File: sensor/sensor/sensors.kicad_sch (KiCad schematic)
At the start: 28 parts, among them IC1 VL53L4CDV0DH_1, J4 Conn_01x03_Socket, J5 Conn_01x03_Socket, J6 Conn_01x03_Socket, J7 Conn_01x03_Socket, U3 APDS-9960, U4 PCA9536DP, U6 ICM-20602

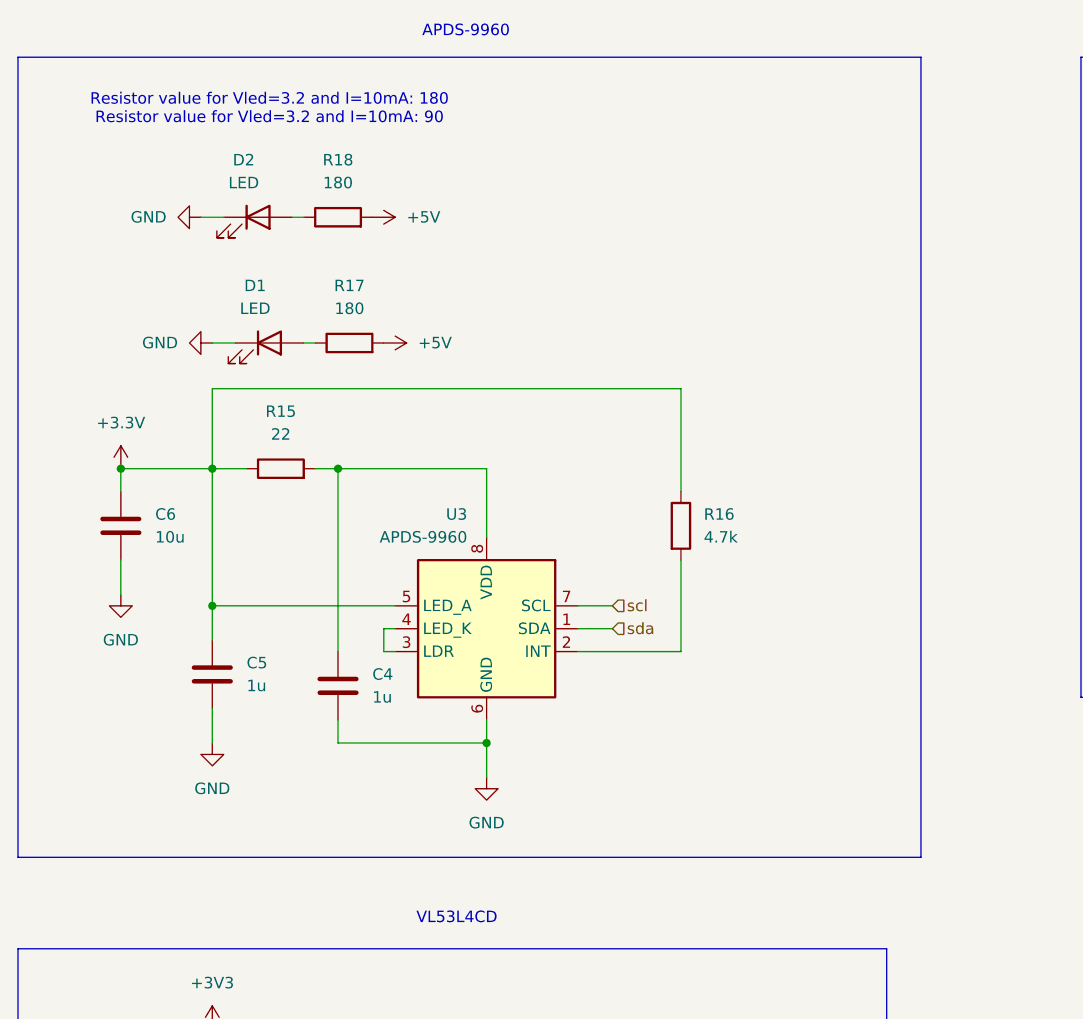
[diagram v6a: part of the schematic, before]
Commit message: update color sensor
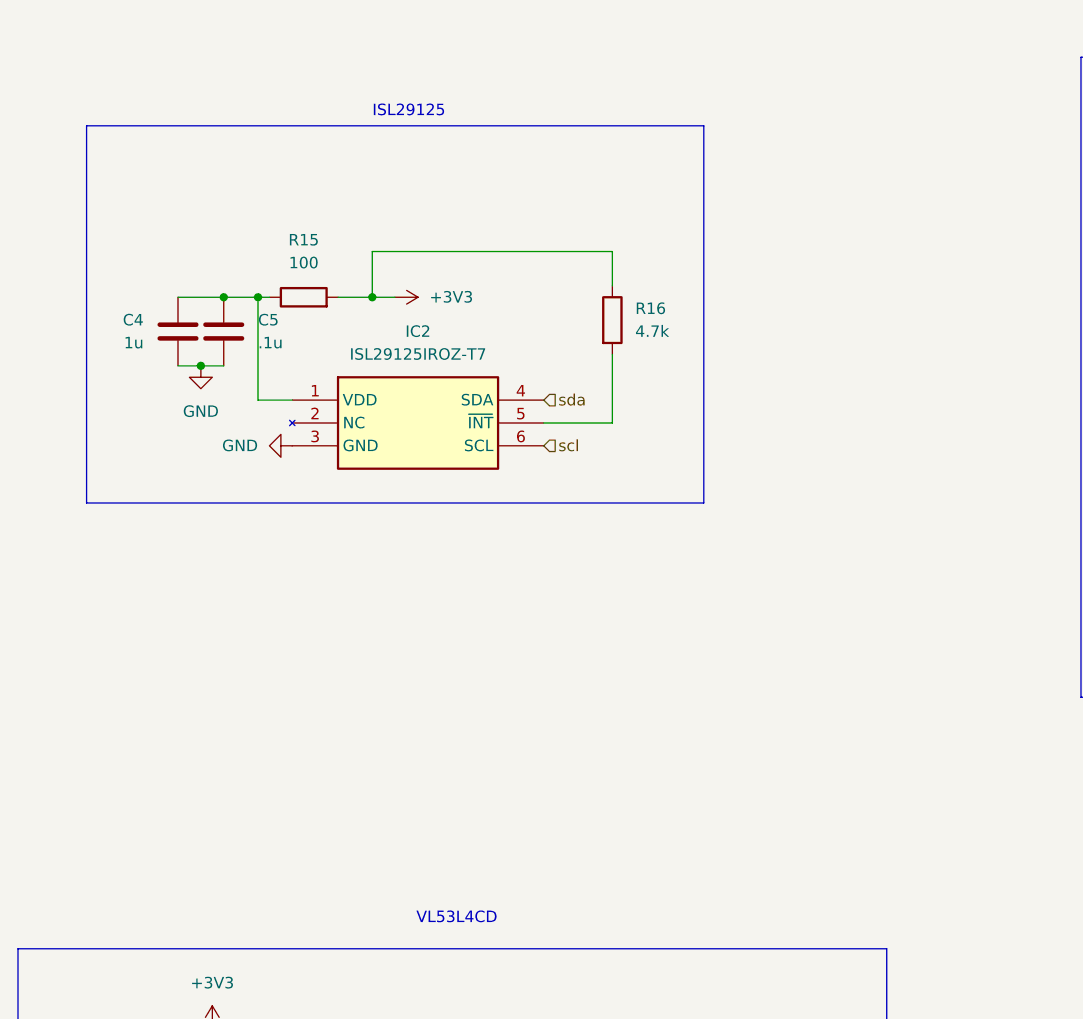
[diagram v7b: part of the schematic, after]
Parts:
- removed C6: 10u, Capacitor_SMD:C_0603_1608Metric_Pad1.08x0.95mm_HandSolder, symbol Device:C
- removed D1, D2: LED, LED_SMD:LED_0805_2012Metric_Pad1.15x1.40mm_HandSolder, symbol Device:LED
- removed R17, R18: 180, Resistor_SMD:R_0402_1005Metric_Pad0.72x0.64mm_HandSolder, symbol Device:R
- removed U3: APDS-9960, Sensor:Avago_APDS-9960, symbol Sensor:APDS-9960
- added IC2: ISL29125IROZ-T7, ISL29125IROZT7, symbol ISL29125:ISL29125IROZ-T7
- C4: footprint Capacitor_SMD:C_0603_1608Metric_Pad1.08x0.95mm_HandSolder -> (none)
- C5: value 1u -> .1u; footprint Capacitor_SMD:C_0603_1608Metric_Pad1.08x0.95mm_HandSolder -> (none)
- R15: value 22 -> 100; footprint Resistor_SMD:R_0402_1005Metric_Pad0.72x0.64mm_HandSolder -> (none)
- R16: footprint Resistor_SMD:R_0402_1005Metric_Pad0.72x0.64mm_HandSolder -> (none)
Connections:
- net +3.3V: no longer C5.1, R15.1, R16.1
- net +3V3: now also R15.2, R16.1
- net GND: now also IC2.3 (GND)
- net scl: now also IC2.6 (SCL)
- net sda: now also IC2.4 (SDA)
- net at R16.2: now also IC2.5 (~{INT})
- net at C4.1: now also C5.1, R15.1, IC2.1 (VDD); no longer R15.2
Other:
- note added: "ISL29125"
- note removed: "APDS-9960"
- note removed: "Resistor value for Vled=3.2 and I=10mA: 180 Resistor value for Vled=3.2 and I=10mA: 90"

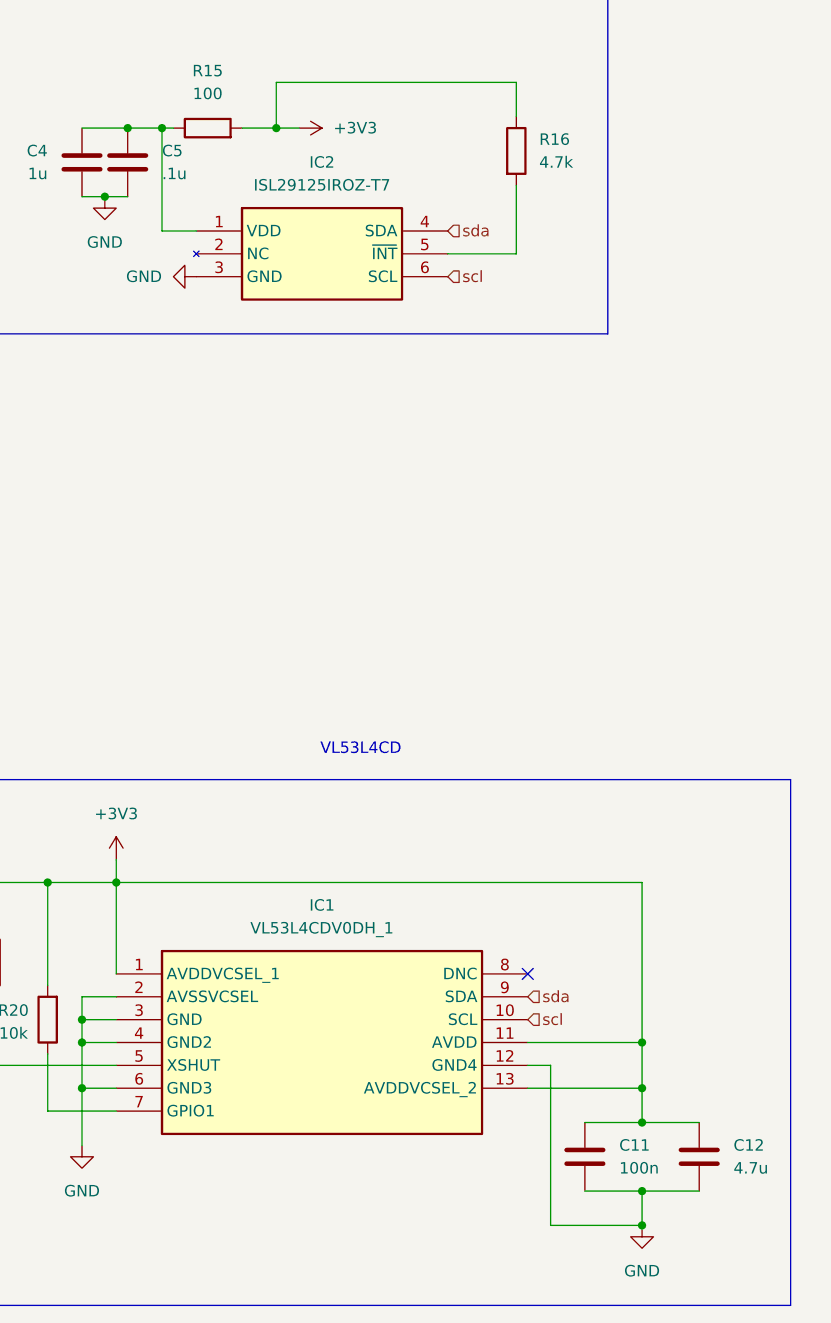
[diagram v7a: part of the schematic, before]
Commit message: added footprints of new sensors and JST/RJ12 connectors into PCB
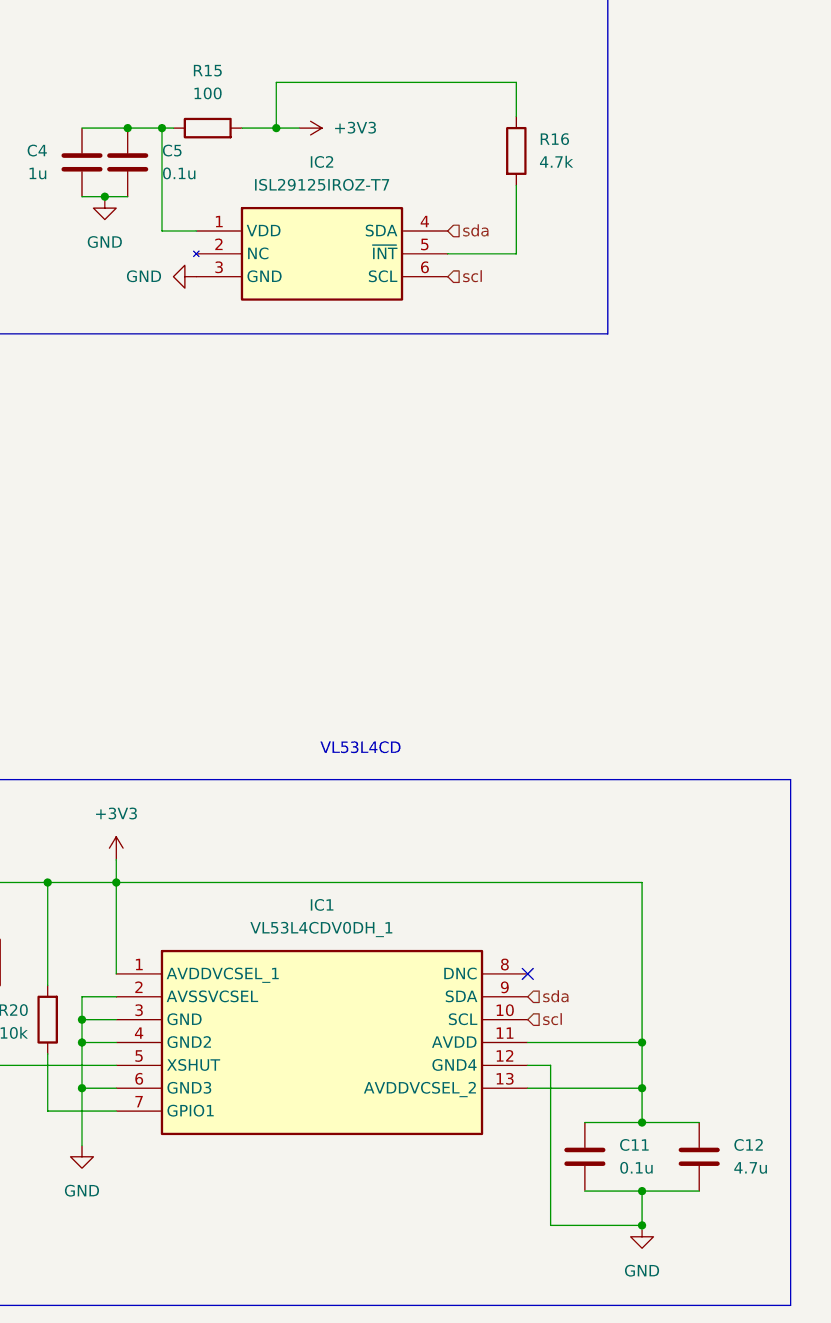
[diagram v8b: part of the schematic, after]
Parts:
- C11: value 100n -> 0.1u; footprint (none) -> Capacitor_SMD:C_0402_1005Metric_Pad0.74x0.62mm_HandSolder
- C12, C4: footprint (none) -> Capacitor_SMD:C_0603_1608Metric_Pad1.08x0.95mm_HandSolder
- C5: value .1u -> 0.1u; footprint (none) -> Capacitor_SMD:C_0402_1005Metric_Pad0.74x0.62mm_HandSolder
- IC1: footprint VL53L4CDV0DH1 -> VL53L4CD:VL53L4CDV0DH1
- IC2: footprint ISL29125IROZT7 -> ISL29125:ISL29125IROZT7
- R15, R16, R20, R21: footprint (none) -> Resistor_SMD:R_0402_1005Metric_Pad0.72x0.64mm_HandSolder
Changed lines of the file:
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@@
 			)
 		)
-		(property "Footprint" ""
+		(property "Footprint" "Capacitor_SMD:C_0603_1608Metric_Pad1.08x0.95mm_HandSolder"
 			(at 43.4848 63.5 0)
 			(effects
@@
 			)
 		)
-		(property "Footprint" ""
+		(property "Footprint" "Resistor_SMD:R_0402_1005Metric_Pad0.72x0.64mm_HandSolder"
 			(at 90.932 58.42 90)
 			(effects
@@
 			)
 		)
-		(property "Value" ".1u"
+		(property "Value" "0.1u"
 			(at 53.34 60.9599 0)
 			(effects
@@
 			)
 		)
-		(property "Footprint" ""
+		(property "Footprint" "Capacitor_SMD:C_0402_1005Metric_Pad0.74x0.62mm_HandSolder"
 			(at 50.4952 63.5 0)
 			(effects
@@
 			)
 		)
-		(property "Footprint" ""
+		(property "Footprint" "Resistor_SMD:R_0402_1005Metric_Pad0.72x0.64mm_HandSolder"
 			(at 42.418 154.94 90)
 			(effects
@@
 			)
 		)
-		(property "Footprint" "ISL29125IROZT7"
+		(property "Footprint" "ISL29125:ISL29125IROZT7"
 			(at 81.28 162.23 0)
 			(effects
@@
 			)
 		)
-		(property "Footprint" ""
+		(property "Footprint" "Capacitor_SMD:C_0603_1608Metric_Pad1.08x0.95mm_HandSolder"
 			(at 113.9952 173.99 0)
 			(effects
@@
 			)
 		)
-		(property "Footprint" ""
+		(property "Footprint" "Resistor_SMD:R_0402_1005Metric_Pad0.72x0.64mm_HandSolder"
 			(at 32.512 148.59 90)
 			(effects
@@
 			)
 		)
-		(property "Value" "100n"
+		(property "Value" "0.1u"
 			(at 104.14 171.4499 0)
 			(effects
@@
 			)
 		)
-		(property "Footprint" ""
+		(property "Footprint" "Capacitor_SMD:C_0402_1005Metric_Pad0.74x0.62mm_HandSolder"
 			(at 101.2952 173.99 0)
 			(effects
@@
 			)
 		)
-		(property "Footprint" ""
+		(property "Footprint" "Resistor_SMD:R_0402_1005Metric_Pad0.72x0.64mm_HandSolder"
 			(at 58.42 57.658 90)
 			(effects
@@
 			)
 		)
-		(property "Footprint" "VL53L4CDV0DH1"
+		(property "Footprint" "VL53L4CD:VL53L4CDV0DH1"
 			(at 90.17 244.78 0)
 			(effects
